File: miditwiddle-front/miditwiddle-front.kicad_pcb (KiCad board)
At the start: 2 copper layers, 98 x 30 mm, 1 part

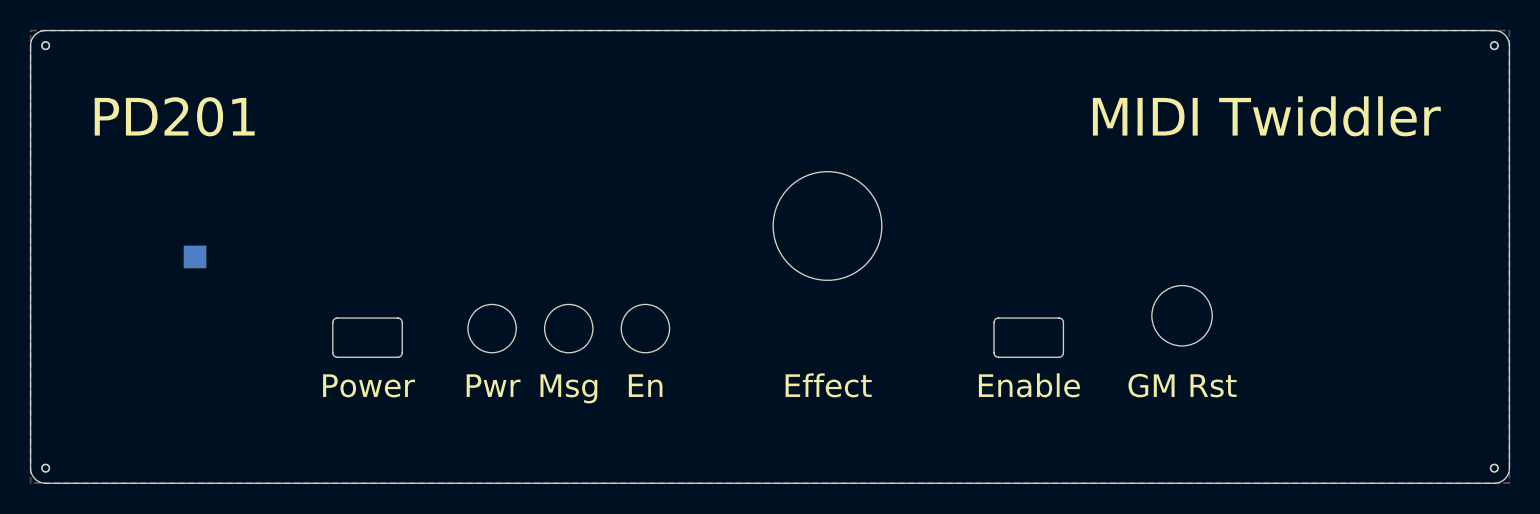
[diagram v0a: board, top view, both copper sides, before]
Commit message: Migrate project to KiCad 6
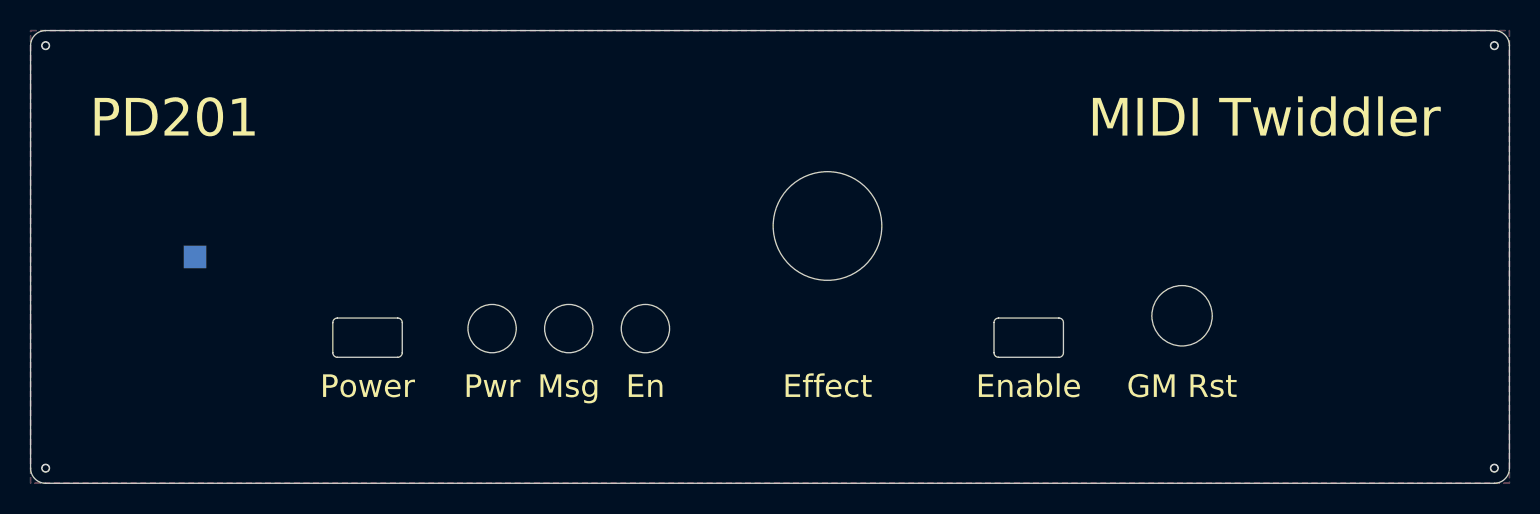
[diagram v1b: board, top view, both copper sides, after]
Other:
- outline, holes or cut-outs redrawn
- net class Default removed
- net class Power removed
